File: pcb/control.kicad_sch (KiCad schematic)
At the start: 4 parts

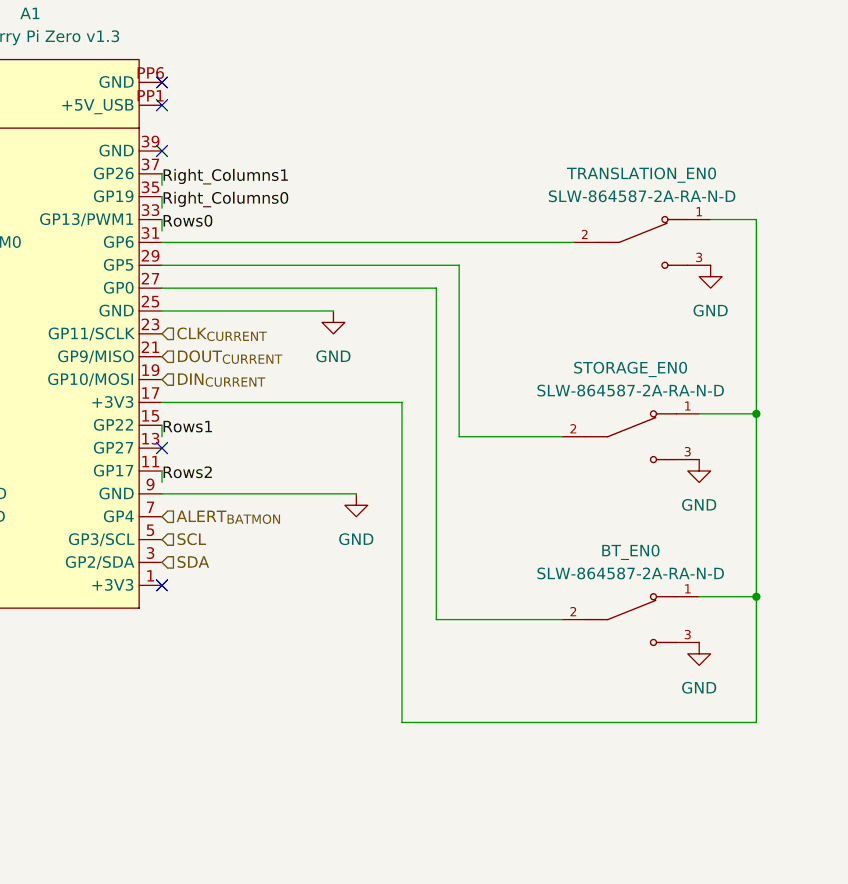
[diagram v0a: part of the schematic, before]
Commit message: Add more ESD protection
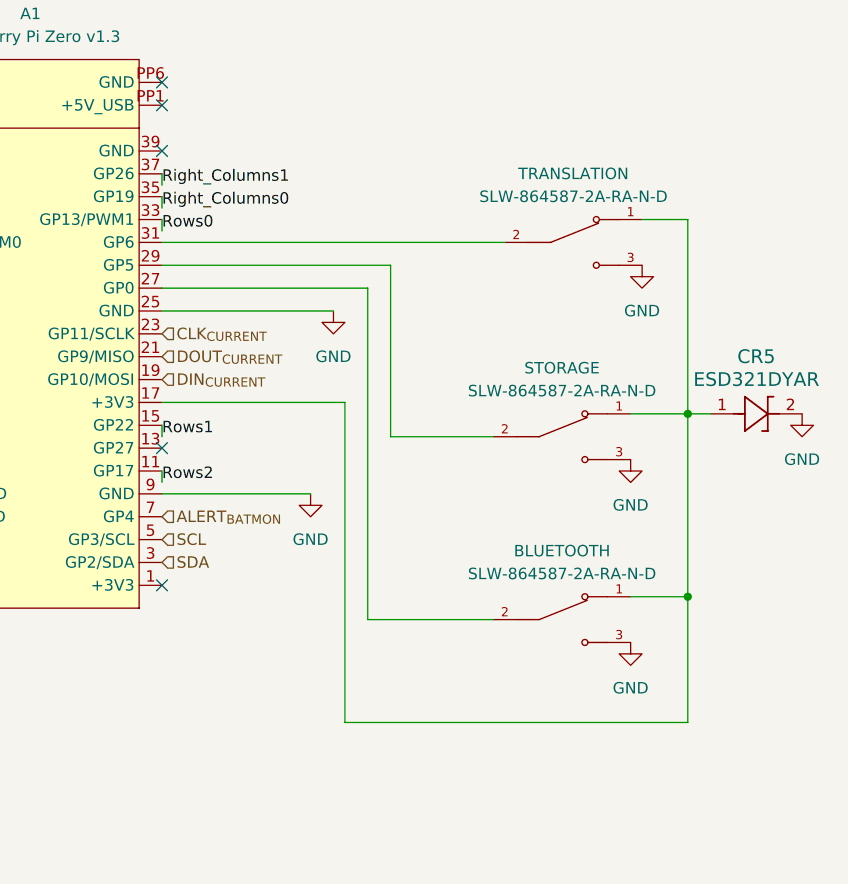
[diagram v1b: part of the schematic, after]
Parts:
- added CR5: ESD321DYAR, SOT5x3_DYA_TEX, symbol ESD321DYAR:ESD321DYAR
- renumbered BT_EN0 to BLUETOOTH, STORAGE_EN0 to STORAGE, TRANSLATION_EN0 to TRANSLATION
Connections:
- net GND: now also CR5.2
- net at A1.17 (+3V3), BLUETOOTH.1, STORAGE.1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: now also CR5.1
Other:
- moved on the sheet: BLUETOOTH, STORAGE, TRANSLATION

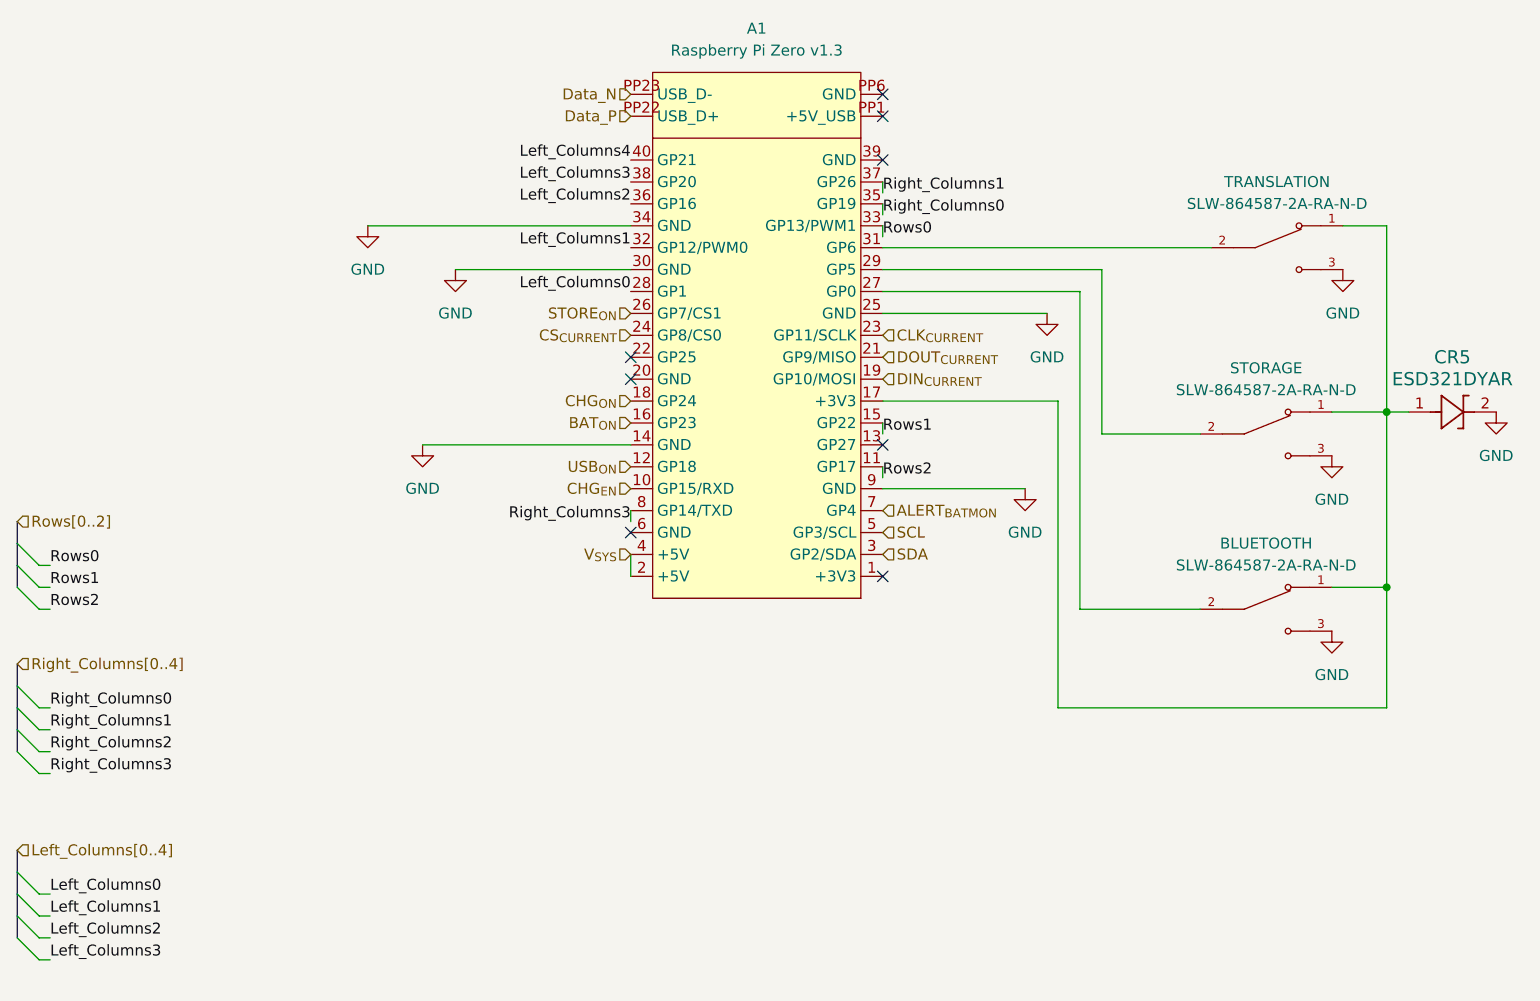
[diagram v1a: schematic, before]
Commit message: Connect right_columns 2 to RPi
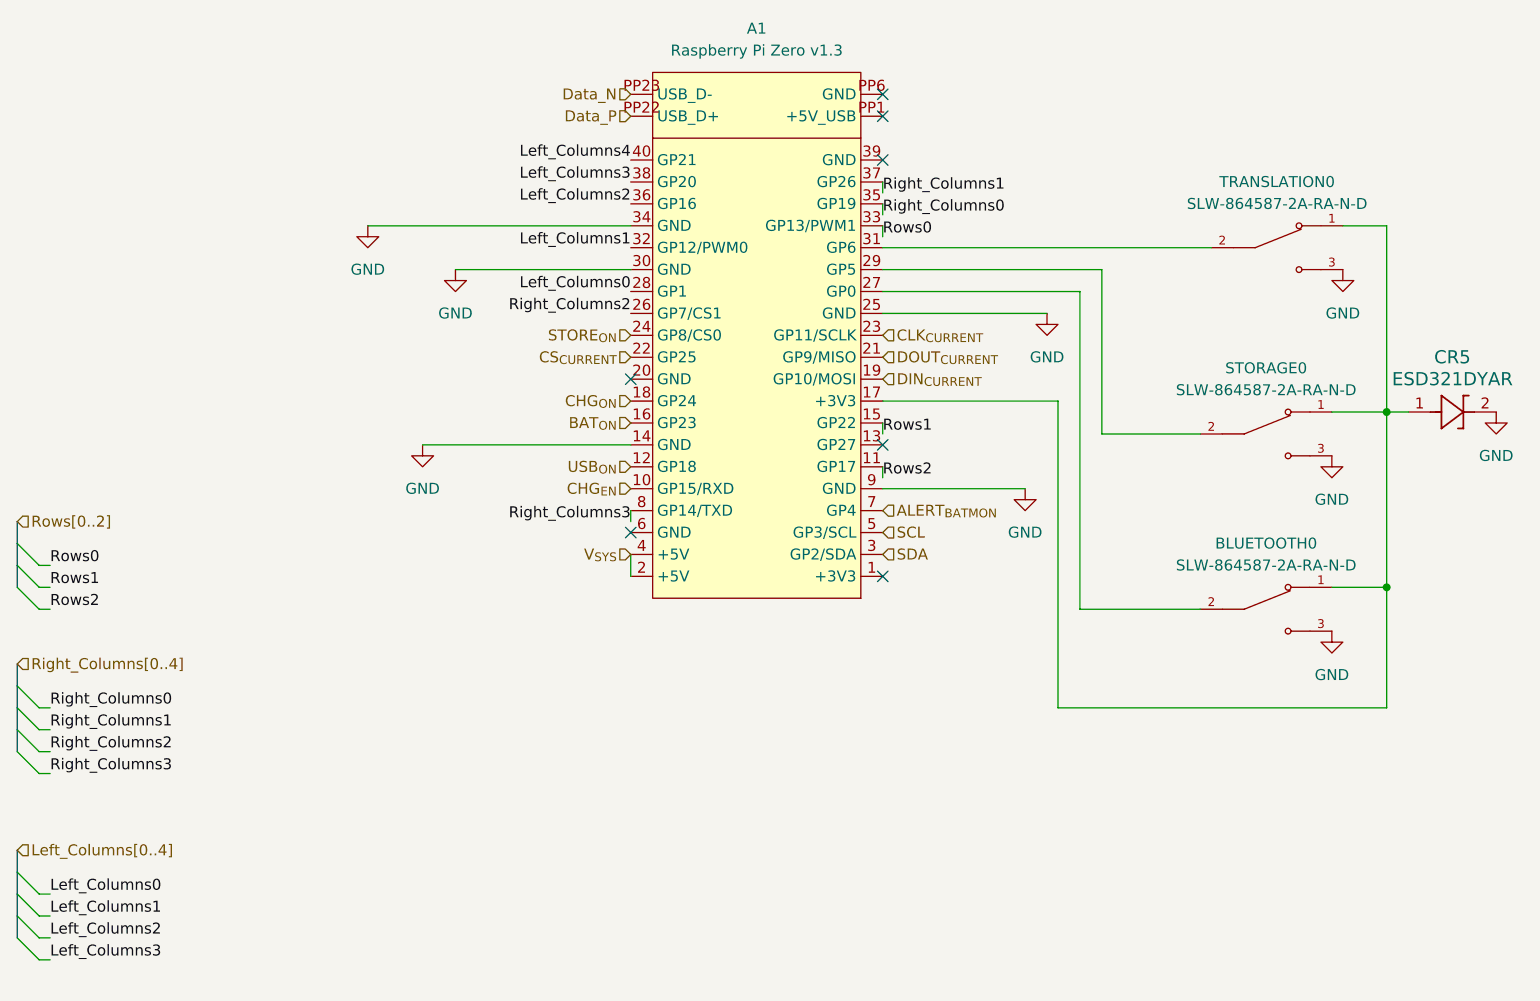
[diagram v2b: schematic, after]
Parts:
- renumbered BLUETOOTH to BLUETOOTH0, STORAGE to STORAGE0, TRANSLATION to TRANSLATION0
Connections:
- net CS_{CURRENT}: now also A1.22 (GP25); no longer A1.24 (GP8/CS0)
- net Right_Columns2: now also A1.26 (GP7/CS1)
- net STORE_{ON}: now also A1.24 (GP8/CS0); no longer A1.26 (GP7/CS1)
- no-connect marks 8 -> 7
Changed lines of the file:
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@@
-	)
-	(no_connect
-		(at 93.98 58.42)
 	)
 	(no_connect
@@
 		)
 	)
+	(label "Right_Columns2"
+		(at 93.98 53.34 180)
+		(effects
+			(font
+				(size 1.27 1.27)
+			)
+			(justify right bottom)
+		)
+	)
 	(label "Left_Columns3"
 		(at 93.98 38.1 180)
@@
 		)
 	)
+	(hierarchical_label "STORE_{ON}"
+		(shape input)
+		(at 93.98 55.88 180)
+		(effects
+			(font
+				(size 1.27 1.27)
+			)
+			(justify right)
+		)
+	)
 	(hierarchical_label "SDA"
 		(shape input)
@@
 	(hierarchical_label "CS_{CURRENT}"
 		(shape input)
-		(at 93.98 55.88 180)
+		(at 93.98 58.42 180)
 		(effects
 			(font
@@
 			)
 			(justify left)
-		)
-	)
-	(hierarchical_label "STORE_{ON}"
-		(shape input)
-		(at 93.98 53.34 180)
-		(effects
-			(font
-				(size 1.27 1.27)
-			)
-			(justify right)
 		)
 	)
@@
 		(dnp no)
 		(fields_autoplaced yes)
-		(property "Reference" "TRANSLATION"
+		(property "Reference" "TRANSLATION0"
 			(at 168.91 38.1 0)
 			(effects
@@
 			(project "right_hand"
 				(path "/efcccfe8-5e20-4b1b-8d3b-61fce771481e/93dd658d-093b-457b-aa9d-06e2289958ef"
-					(reference "TRANSLATION")
+					(reference "TRANSLATION0")
 					(unit 1)
 				)
@@
 		(dnp no)
 		(fields_autoplaced yes)
-		(property "Reference" "STORAGE"
+		(property "Reference" "STORAGE0"
 			(at 167.64 59.69 0)
 			(effects
@@
 			(project "right_hand"
 				(path "/efcccfe8-5e20-4b1b-8d3b-61fce771481e/93dd658d-093b-457b-aa9d-06e2289958ef"
-					(reference "STORAGE")
+					(reference "STORAGE0")
 					(unit 1)
 				)
@@
 		(dnp no)
 		(fields_autoplaced yes)
-		(property "Reference" "BLUETOOTH"
+		(property "Reference" "BLUETOOTH0"
 			(at 167.64 80.01 0)
 			(effects
@@
 			(project "right_hand"
 				(path "/efcccfe8-5e20-4b1b-8d3b-61fce771481e/93dd658d-093b-457b-aa9d-06e2289958ef"
-					(reference "BLUETOOTH")
+					(reference "BLUETOOTH0")
 					(unit 1)
 				)

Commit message: Update PCB to connect 4th right column
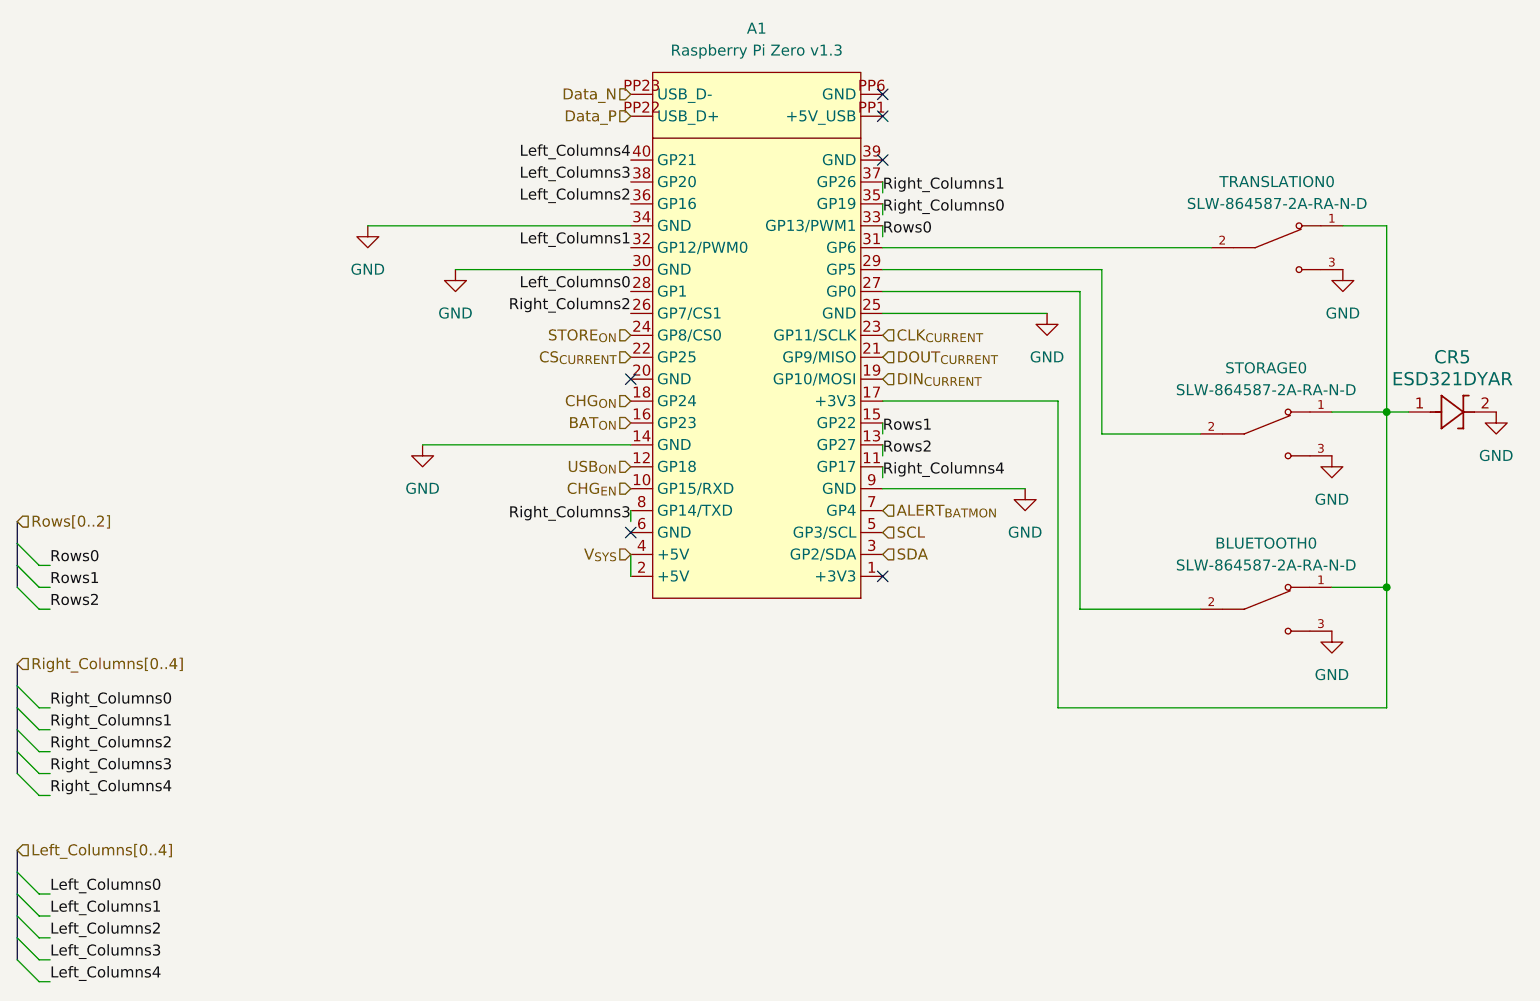
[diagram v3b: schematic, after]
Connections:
- net Rows2: now also A1.13 (GP27); no longer A1.11 (GP17)
- new net Right_Columns4: A1.11 (GP17)
- no-connect marks 7 -> 6
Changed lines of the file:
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@@
-	)
-	(no_connect
-		(at 123.19 68.58)
 	)
 	(no_connect
@@
 	)
 	(bus_entry
+		(at 22.86 128.27)
+		(size 2.54 2.54)
+		(stroke
+			(width 0)
+			(type default)
+		)
+	)
+	(bus_entry
 		(at 22.86 118.11)
 		(size 2.54 2.54)
@@
 	)
 	(bus_entry
+		(at 22.86 106.68)
+		(size 2.54 2.54)
+		(stroke
+			(width 0)
+			(type default)
+		)
+	)
+	(bus_entry
 		(at 22.86 125.73)
 		(size 2.54 2.54)
@@
 	(bus
 		(pts
+			(xy 22.86 104.14) (xy 22.86 106.68)
+		)
+		(stroke
+			(width 0)
+			(type default)
+		)
+	)
+	(bus
+		(pts
 			(xy 22.86 115.57) (xy 22.86 118.11)
 		)
@@
 		)
 	)
+	(wire
+		(pts
+			(xy 123.19 69.85) (xy 123.19 68.58)
+		)
+		(stroke
+			(width 0)
+			(type default)
+		)
+	)
 	(bus
 		(pts
@@
 	(wire
 		(pts
+			(xy 25.4 130.81) (xy 26.67 130.81)
+		)
+		(stroke
+			(width 0)
+			(type default)
+		)
+	)
+	(wire
+		(pts
 			(xy 93.98 81.28) (xy 93.98 83.82)
 		)
@@
 	(wire
 		(pts
+			(xy 181.61 85.09) (xy 181.61 64.77)
+		)
+		(stroke
+			(width 0)
+			(type default)
+		)
+	)
+	(wire
+		(pts
+			(xy 175.26 64.77) (xy 181.61 64.77)
+		)
+		(stroke
+			(width 0)
+			(type default)
+		)
+	)
+	(wire
+		(pts
 			(xy 123.19 72.39) (xy 123.19 71.12)
 		)
@@
 	(wire
 		(pts
-			(xy 181.61 85.09) (xy 181.61 64.77)
-		)
-		(stroke
-			(width 0)
-			(type default)
-		)
-	)
-	(wire
-		(pts
-			(xy 175.26 64.77) (xy 181.61 64.77)
-		)
-		(stroke
-			(width 0)
-			(type default)
-		)
-	)
-	(wire
-		(pts
 			(xy 123.19 45.72) (xy 161.29 45.72)
 		)
@@
 	(wire
 		(pts
+			(xy 25.4 109.22) (xy 26.67 109.22)
+		)
+		(stroke
+			(width 0)
+			(type default)
+		)
+	)
+	(wire
+		(pts
 			(xy 123.19 48.26) (xy 148.59 48.26)
 		)
@@
 		(pts
 			(xy 181.61 99.06) (xy 181.61 85.09)
+		)
+		(stroke
+			(width 0)
+			(type default)
+		)
+	)
+	(bus
+		(pts
+			(xy 22.86 125.73) (xy 22.86 128.27)
 		)
 		(stroke
@@
 		)
 	)
+	(label "Right_Columns4"
+		(at 26.67 109.22 0)
+		(effects
+			(font
+				(size 1.27 1.27)
+			)
+			(justify left bottom)
+		)
+	)
 	(label "Left_Columns1"
 		(at 93.98 45.72 180)
@@
 		)
 	)
+	(label "Left_Columns4"
+		(at 26.67 130.81 0)
+		(effects
+			(font
+				(size 1.27 1.27)
+			)
+			(justify left bottom)
+		)
+	)
 	(label "Right_Columns0"
 		(at 26.67 99.06 0)
@@
 		)
 	)
+	(label "Right_Columns4"
+		(at 123.19 72.39 0)
+		(effects
+			(font
+				(size 1.27 1.27)
+			)
+			(justify left bottom)
+		)
+	)
 	(label "Rows2"
-		(at 123.19 72.39 0)
-		(effects
-			(font
+		(at 123.19 69.85 0)
+		(effects
+			(font
